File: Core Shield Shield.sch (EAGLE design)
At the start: 10 parts, among them IC1 MC33269T-5.0

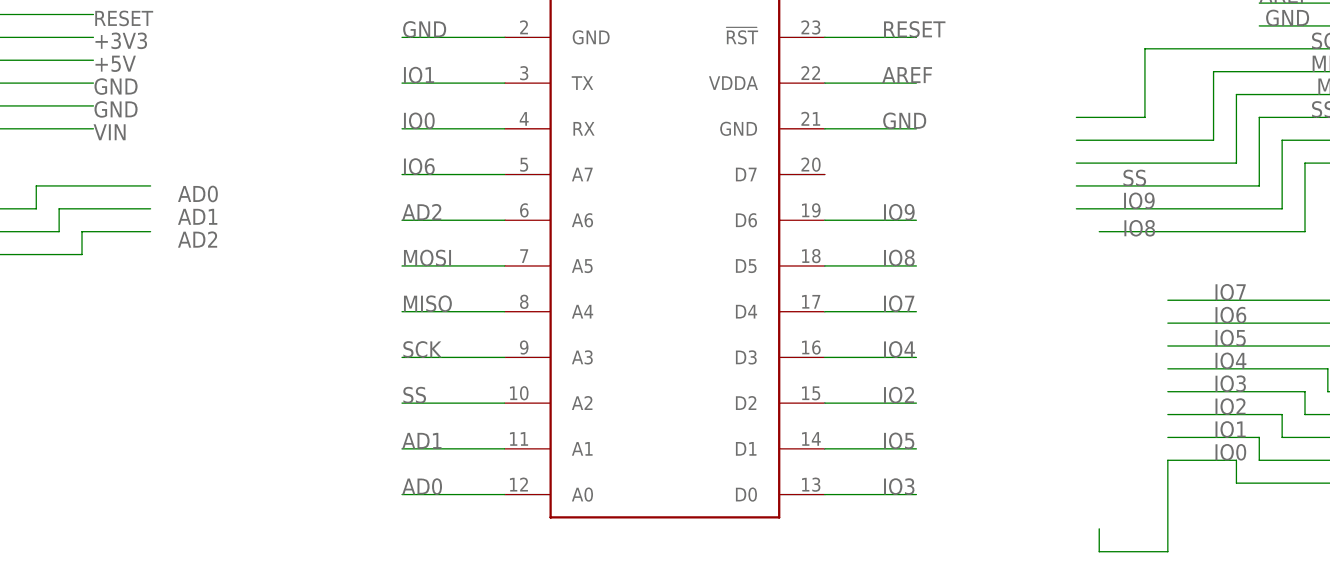
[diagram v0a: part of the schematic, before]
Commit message: Re-routed traces
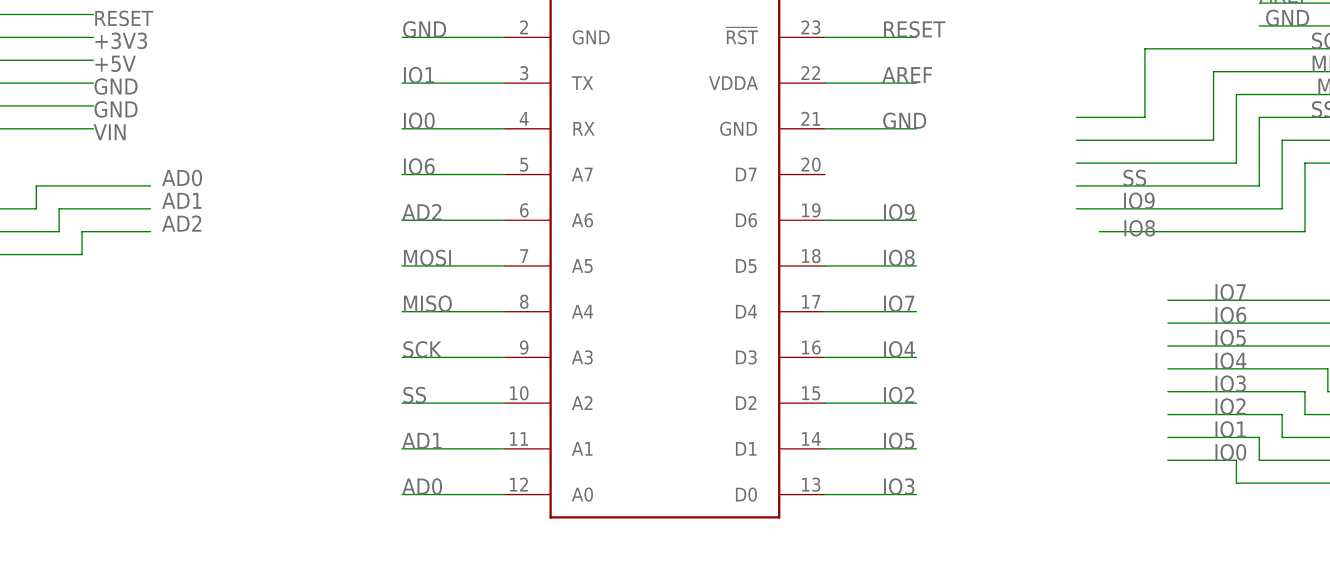
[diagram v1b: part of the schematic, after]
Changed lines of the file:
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@@
 <setting verticaltext="up"/>
 </settings>
-<grid distance="0.1" unitdist="inch" unit="inch" style="lines" multiple="1" display="no" altdistance="0.01" altunitdist="inch" altunit="inch"/>
+<grid distance="0.05" unitdist="inch" unit="inch" style="lines" multiple="1" display="yes" altdistance="0.005" altunitdist="inch" altunit="inch"/>
 <layers>
 <layer number="1" name="Top" color="4" fill="1" visible="no" active="no"/>
@@
 <wire x1="39.37" y1="69.85" x2="39.37" y2="72.39" width="0.1524" layer="91"/>
 <wire x1="39.37" y1="72.39" x2="52.07" y2="72.39" width="0.1524" layer="91"/>
-<label x="59.69" y="72.39" size="1.778" layer="95" rot="R180"/>
+<label x="53.34" y="72.39" size="1.778" layer="95"/>
 <pinref part="AD" gate="A" pin="1"/>
 </segment>
@@
 <wire x1="41.91" y1="69.85" x2="41.91" y2="67.31" width="0.1524" layer="91"/>
 <wire x1="41.91" y1="67.31" x2="29.21" y2="67.31" width="0.1524" layer="91"/>
-<label x="59.69" y="69.85" size="1.778" layer="95" rot="R180"/>
+<label x="53.34" y="69.85" size="1.778" layer="95"/>
 <pinref part="AD" gate="A" pin="2"/>
 </segment>
@@
 <wire x1="44.45" y1="64.77" x2="44.45" y2="67.31" width="0.1524" layer="91"/>
 <wire x1="44.45" y1="67.31" x2="52.07" y2="67.31" width="0.1524" layer="91"/>
-<label x="59.69" y="67.31" size="1.778" layer="95" rot="R180"/>
+<label x="53.34" y="67.31" size="1.778" layer="95"/>
 <pinref part="AD" gate="A" pin="3"/>
 </segment>
@@
 <wire x1="172.72" y1="39.37" x2="172.72" y2="41.91" width="0.1524" layer="91"/>
 <wire x1="172.72" y1="41.91" x2="165.1" y2="41.91" width="0.1524" layer="91"/>
-<wire x1="165.1" y1="41.91" x2="165.1" y2="31.75" width="0.1524" layer="91"/>
-<wire x1="165.1" y1="31.75" x2="157.48" y2="31.75" width="0.1524" layer="91"/>
-<wire x1="157.48" y1="34.29" x2="157.48" y2="31.75" width="0.1524" layer="91"/>
 <label x="170.18" y="41.91" size="1.778" layer="95"/>
 <pinref part="IOL" gate="A" pin="1"/>
